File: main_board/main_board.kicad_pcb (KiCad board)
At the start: 2 copper layers, 68.3 x 56.9 mm, 41 parts, among them J2 2-1734248-0, P1 USB_C_Plug_USB2.0, P2 USB_C_Plug_USB2.0, SW1 SW_Push_Open, U1 LM7805_TO220, U2 ESP32-S3-WROOM-2, U3 MCP1700x-330xxTT, U4 CH224K

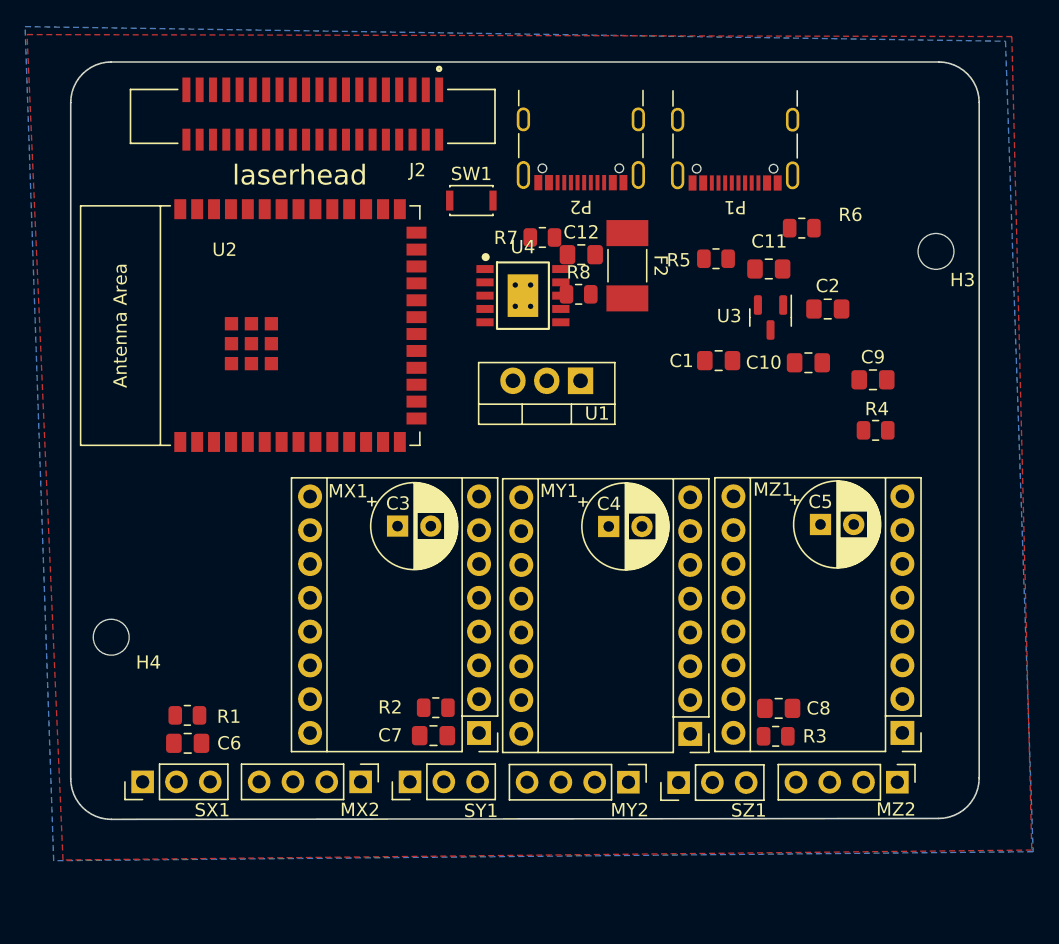
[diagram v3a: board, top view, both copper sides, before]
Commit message: updated step models
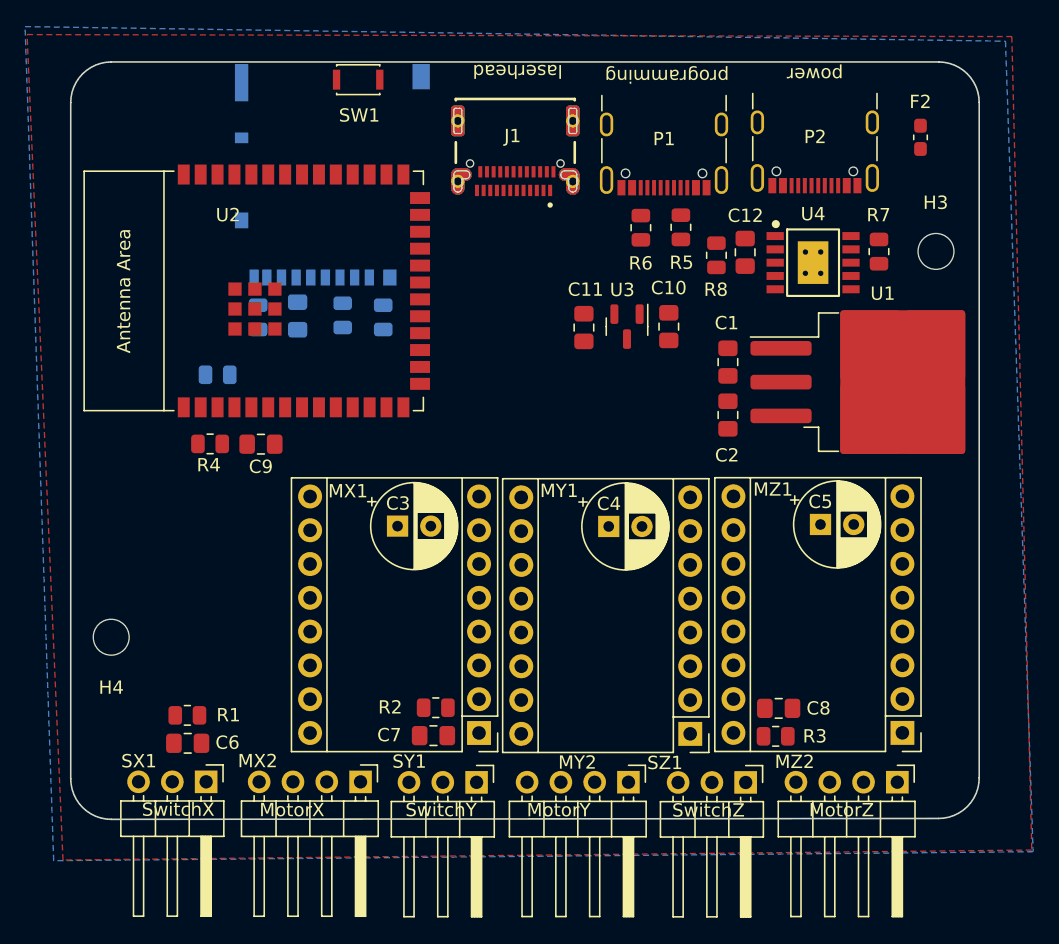
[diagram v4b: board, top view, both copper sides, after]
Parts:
- removed J2: 2-1734248-0, footprints:TE_2-1734248-0
- added C13: 0.1U, Capacitor_SMD:C_0805_2012Metric_Pad1.18x1.45mm_HandSolder, B.Cu at (175.9, 136.8)
- added J1: USB_C_Receptacle, footprints:GCT_USB4080-03-A_REVA1, F.Cu at (192.3, 126.7)
- added J3: Micro_SD_Card_Det_Hirose_DM3AT, footprints:microSD_HC_Hirose_DM3AT-SF-PEJM5, B.Cu at (178.6, 126.2)
- added R10: 10K, Resistor_SMD:R_0805_2012Metric, B.Cu at (179.3, 136.8)
- added R11: 10K, Resistor_SMD:R_0805_2012Metric, B.Cu at (173.0, 136.9)
- added R12: 10K, Resistor_SMD:R_0805_2012Metric, B.Cu at (182.4, 136.9)
- added R9: 10K, Resistor_SMD:R_0805_2012Metric, B.Cu at (169.9, 141.2)
- F2: footprint Fuse:Fuse_Littelfuse-NANO2-451_453 -> Fuse:Fuse_0603_1608Metric_Pad1.05x0.95mm_HandSolder
- MX2, MY2, MZ2: footprint Connector_PinHeader_2.54mm:PinHeader_1x04_P2.54mm_Vertical -> Connector_PinHeader_2.54mm:PinHeader_1x04_P2.54mm_Horizontal
- SX1, SY1, SZ1: footprint Connector_PinHeader_2.54mm:PinHeader_1x03_P2.54mm_Vertical -> Connector_PinHeader_2.54mm:PinHeader_1x03_P2.54mm_Horizontal
- U1: value LM7805_TO220 -> LM7805_TO263; footprint Package_TO_SOT_THT:TO-220-3_Vertical -> Package_TO_SOT_SMD:TO-263-3_TabPin2
- moved R4 50.0 mm to (169.4, 146.4), turned to 0 degrees
- moved C9 46.3 mm to (173.2, 146.4), turned to 0 degrees
- moved R7 25.3 mm to (219.6, 132.0), turned to -90 degrees
- moved F2 24.1 mm to (222.8, 123.4), turned to 90 degrees
- moved U1 22.7 mm to (219.9, 141.8), turned to 0 degrees
- moved U4 22.0 mm to (214.7, 132.8)
- moved P2 17.6 mm to (214.8, 123.3)
- moved C11 14.6 mm to (197.5, 137.7), turned to -90 degrees
- moved SW1 12.4 mm to (180.5, 119.0)
- moved C12 12.3 mm to (209.6, 132.0), turned to -90 degrees
- moved R6 12.1 mm to (201.7, 130.2), turned to -90 degrees
- moved C2 10.9 mm to (208.3, 144.2), turned to 90 degrees
- moved C10 10.8 mm to (203.8, 137.6), turned to -90 degrees
- moved U3 10.8 mm to (200.7, 137.6)
- moved R8 10.8 mm to (207.4, 132.2), turned to -90 degrees
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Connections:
- net SPI_SS3 renamed SPI_SS_MOTOR
- R7 pad 1: VBUS -> +12V
- SX1 pad 1: +3.3V -> GND
- SX1 pad 3: GND -> +3.3V
- SY1 pad 1: +3.3V -> GND
- SY1 pad 3: GND -> +3.3V
- SZ1 pad 1: +3.3V -> GND
- SZ1 pad 3: GND -> +3.3V
- U2 pad 11: unconnected-(U2-GPIO18/U1RXD/ADC2_CH7/CLK_OUT3-Pad11) -> Z_PO
- U2 pad 18: SPI_SS -> SPI_SS_FLASH
- U2 pad 22: SPI_SS2 -> SPI_SS_FPGA
- U2 pad 23: unconnected-(U2-GPIO21-Pad23) -> Z_DIR
- U2 pad 31: unconnected-(U2-GPIO38/FSPIWP/SUBSPIWP-Pad31) -> Z_STEP
- U2 pad 4: unconnected-(U2-GPIO4/TOUCH4/ADC1_CH3-Pad4) -> SD_CLK
- U2 pad 5: unconnected-(U2-GPIO5/TOUCH5/ADC1_CH4-Pad5) -> SD_MISO
- U2 pad 6: unconnected-(U2-GPIO6/TOUCH6/ADC1_CH5-Pad6) -> SD_MOSI
- U2 pad 7: unconnected-(U2-GPIO7/TOUCH7/ADC1_CH6-Pad7) -> SD_SS
- U4 pad 0: (no net) -> GND
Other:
- board text added: "MotorX"
- board text added: "MotorY"
- board text added: "MotorZ"
- board text added: "SwitchX"
- board text added: "SwitchY"
- board text added: "SwitchZ"
- board text added: "power"
- board text added: "programming"

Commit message: routed main board
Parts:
- C3, C4, C5: footprint Capacitor_THT:CP_Radial_D6.3mm_P2.50mm -> footprints:CP_Radial_D6.3mm_P2.50mm
- moved C9 4.52 mm to (169.2, 148.6), turned to 180 degrees
- moved C13 0.30 mm to (175.9, 137.1)
- moved R12 0.24 mm to (182.2, 136.8)
- turned F2 to -90 degrees
- turned R3 to 180 degrees
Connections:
- J1 pad A11: Y_PO -> SPI_SS_FPGA
- J1 pad A6: SPI_SS_FPGA -> Y_PO
- J1 pad A7: SPI_SCK -> X_STEP
- J1 pad A8: CFG_DONE -> CFG_RST
- J1 pad B10: X_PO -> SPI_SS_FLASH
- J1 pad B11: X_STEP -> SPI_SCK
- J1 pad B2: Y_STEP -> CFG_DONE
- J1 pad B6: CFG_RST -> Y_STEP
- J1 pad B7: SPI_SS_FLASH -> X_PO
- MX2 pad 1: X_2B -> X_1B
- MX2 pad 2: X_2A -> X_1A
- MX2 pad 3: X_1A -> X_2A
- MX2 pad 4: X_1B -> X_2B
- MY2 pad 1: Y_2B -> Y_1B
- MY2 pad 2: Y_2A -> Y_1A
- MY2 pad 3: Y_1A -> Y_2A
- MY2 pad 4: Y_1B -> Y_2B
- MZ2 pad 1: Z_2B -> Z_1B
- MZ2 pad 2: Z_2A -> Z_1A
- MZ2 pad 3: Z_1A -> Z_2A
- MZ2 pad 4: Z_1B -> Z_2B
- U2 pad 10: FREE -> unconnected-(U2-GPIO17/U1TXD/ADC2_CH6-Pad10)
- U2 pad 12: POT_SDA -> unconnected-(U2-GPIO8/TOUCH8/ADC1_CH7/SUBSPICS1-Pad12)
- U2 pad 17: POT_SCL -> STEP_ENABLE
- U2 pad 18: SPI_SS_FLASH -> POT_SCL
- U2 pad 22: SPI_SS_FPGA -> unconnected-(U2-GPIO14/TOUCH14/ADC2_CH3/FSPIWP/FSPIDQS/SUBSPIWP-Pad22)
- U2 pad 24: unconnected-(U2-GPIO47/SPICLK_P/SUBSPICLK_P_DIFF-Pad24) -> CFG_RST
- U2 pad 25: unconnected-(U2-GPIO48/SPICLK_N/SUBSPICLK_N_DIFF-Pad25) -> POT_SDA
- U2 pad 26: unconnected-(U2-GPIO45-Pad26) -> SPI_SS_FPGA
- U2 pad 31: Z_STEP -> CFG_DONE
- U2 pad 32: STEP_ENABLE -> FREE
- U2 pad 33: unconnected-(U2-MTDO/GPIO40/CLK_OUT2-Pad33) -> SPI_SS_FLASH
- U2 pad 36: CFG_RST -> unconnected-(U2-U0RXD/GPIO44/CLK_OUT2-Pad36)
- U2 pad 37: CFG_DONE -> Z_STEP
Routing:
- net +3.3V: track 0.00 -> 210.0 mm, vias 0 -> 5
- net +12V: track 0.00 -> 167.5 mm, vias 0 -> 3
- net Z_STEP: track 0.00 -> 101.7 mm
- net SPI_SCK: track 0.00 -> 85.4 mm, vias 0 -> 3
- net X_PO: track 0.00 -> 80.5 mm, vias 0 -> 1
- net SPI_SS_MOTOR: track 0.00 -> 74.2 mm
- net Y_PO: track 0.00 -> 71.9 mm, vias 0 -> 1
- net SPI_SO: track 0.00 -> 64.2 mm, vias 0 -> 3
- net Z_PO: track 0.00 -> 61.6 mm
- net STEP_ENABLE: track 0.00 -> 56.3 mm, vias 0 -> 1
- net Z_DIR: track 0.00 -> 54.3 mm, vias 0 -> 1
- net X_DIR: track 0.00 -> 53.5 mm, vias 0 -> 1
- net Y_DIR: track 0.00 -> 49.5 mm, vias 0 -> 2
- net X_STEP: track 0.00 -> 46.7 mm, vias 0 -> 1
- net Y_STEP: track 0.00 -> 46.2 mm, vias 0 -> 2
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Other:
- board text removed: "MotorX"
- board text removed: "MotorY"
- board text removed: "MotorZ"
- board text removed: "SwitchX"
- board text removed: "SwitchY"
- board text removed: "SwitchZ"

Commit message: updated design
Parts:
- moved C3 15.6 mm to (168.8, 157.8)
- moved C5 14.8 mm to (202.5, 144.9)
- moved G1 13.7 mm to (206.0, 138.7)
- moved R3 13.1 mm to (224.9, 167.9), turned to 0 degrees
- moved C8 13.0 mm to (225.0, 165.0)
- moved R2 12.9 mm to (173.5, 166.2)
- moved C7 12.8 mm to (173.3, 168.7)
- moved C4 8.62 mm to (195.5, 144.9)
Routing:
- net +12V: track 167.5 -> 204.9 mm, vias 3 -> 4
- net Z_PO: track 61.6 -> 86.0 mm
- net +3.3V: track 210.0 -> 192.6 mm
- net Y_PO: track 71.9 -> 88.7 mm
- net STEP_ENABLE: track 56.3 -> 54.0 mm
- net SPI_SO: track 64.2 -> 64.9 mm
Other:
- board text added: "PCB3D_BR_main_board"
- board text added: "PCB3D_TL_main_board"
